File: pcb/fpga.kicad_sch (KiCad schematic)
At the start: 0 parts

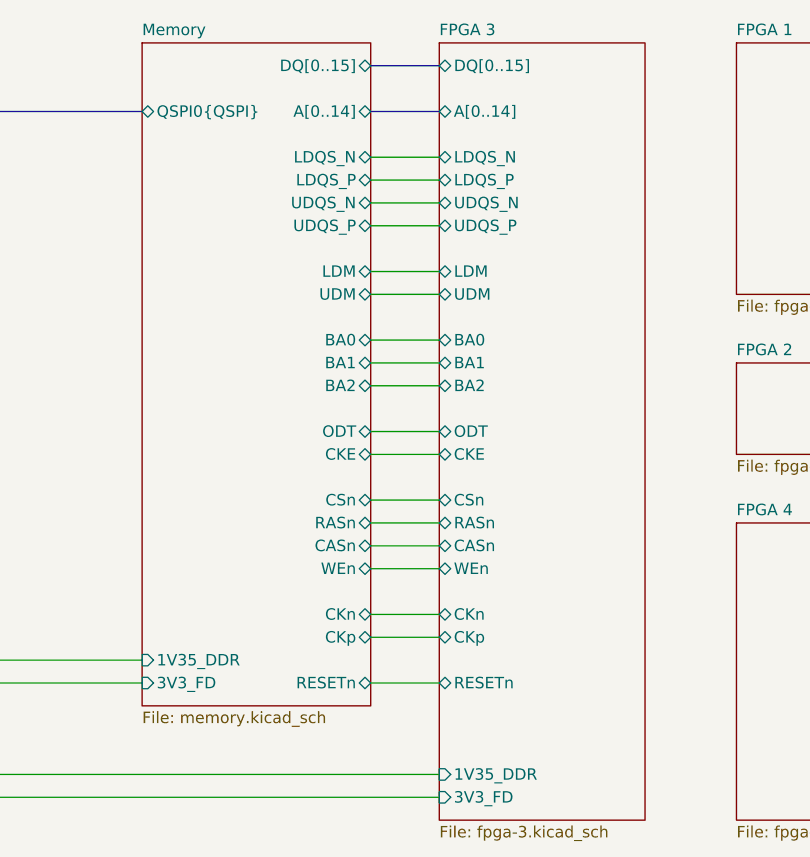
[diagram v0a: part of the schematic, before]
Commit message: added mig ddr pinout constraints
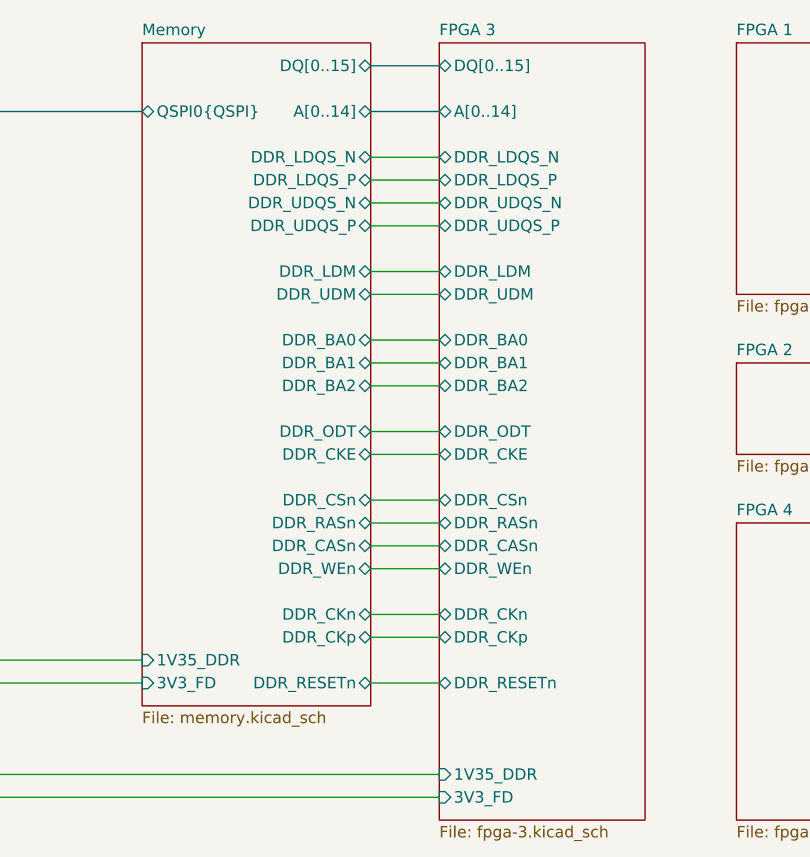
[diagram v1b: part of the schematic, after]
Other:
- sheet FPGA 3 ports: added DDR_BA0, DDR_BA1, DDR_BA2, DDR_CASn, DDR_CKE, DDR_CKn, DDR_CKp, DDR_CSn, DDR_LDM, DDR_LDQS_N, DDR_LDQS_P, DDR_ODT, DDR_RASn, DDR_RESETn, DDR_UDM, DDR_UDQS_N, DDR_UDQS_P, DDR_WEn; removed BA0, BA1, BA2, CASn, CKE, CKn, CKp, CSn, LDM, LDQS_N, LDQS_P, ODT, RASn, RESETn, UDM, UDQS_N, UDQS_P, WEn
- sheet Memory ports: added DDR_BA0, DDR_BA1, DDR_BA2, DDR_CASn, DDR_CKE, DDR_CKn, DDR_CKp, DDR_CSn, DDR_LDM, DDR_LDQS_N, DDR_LDQS_P, DDR_ODT, DDR_RASn, DDR_RESETn, DDR_UDM, DDR_UDQS_N, DDR_UDQS_P, DDR_WEn; removed BA0, BA1, BA2, CASn, CKE, CKn, CKp, CSn, LDM, LDQS_N, LDQS_P, ODT, RASn, RESETn, UDM, UDQS_N, UDQS_P, WEn
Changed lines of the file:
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@@
 			)
 		)
-		(pin "BA0" bidirectional
+		(pin "DDR_BA0" bidirectional
 			(at 132.08 86.36 180)
 			(effects
@@
 			)
 		)
-		(pin "BA1" bidirectional
+		(pin "DDR_BA1" bidirectional
 			(at 132.08 88.9 180)
 			(effects
@@
 			)
 		)
-		(pin "BA2" bidirectional
+		(pin "DDR_BA2" bidirectional
 			(at 132.08 91.44 180)
 			(effects
@@
 			)
 		)
-		(pin "CASn" bidirectional
+		(pin "DDR_CASn" bidirectional
 			(at 132.08 109.22 180)
 			(effects
@@
 			)
 		)
-		(pin "CKE" bidirectional
+		(pin "DDR_CKE" bidirectional
 			(at 132.08 99.06 180)
 			(effects
@@
 			)
 		)
-		(pin "CKn" bidirectional
+		(pin "DDR_CKn" bidirectional
 			(at 132.08 116.84 180)
 			(effects
@@
 			)
 		)
-		(pin "CKp" bidirectional
+		(pin "DDR_CKp" bidirectional
 			(at 132.08 119.38 180)
 			(effects
@@
 			)
 		)
-		(pin "CSn" bidirectional
+		(pin "DDR_CSn" bidirectional
 			(at 132.08 104.14 180)
 			(effects
@@
 			)
 		)
-		(pin "LDM" bidirectional
+		(pin "DDR_LDM" bidirectional
 			(at 132.08 78.74 180)
 			(effects
@@
 			)
 		)
-		(pin "LDQS_N" bidirectional
+		(pin "DDR_LDQS_N" bidirectional
 			(at 132.08 66.04 180)
 			(effects
@@
 			)
 		)
-		(pin "LDQS_P" bidirectional
+		(pin "DDR_LDQS_P" bidirectional
 			(at 132.08 68.58 180)
 			(effects
@@
 			)
 		)
-		(pin "ODT" bidirectional
+		(pin "DDR_ODT" bidirectional
 			(at 132.08 96.52 180)
 			(effects
@@
 			)
 		)
-		(pin "RASn" bidirectional
+		(pin "DDR_RASn" bidirectional
 			(at 132.08 106.68 180)
 			(effects
@@
 			)
 		)
-		(pin "RESETn" bidirectional
+		(pin "DDR_RESETn" bidirectional
 			(at 132.08 124.46 180)
 			(effects
@@
 			)
 		)
-		(pin "UDM" bidirectional
+		(pin "DDR_UDM" bidirectional
 			(at 132.08 81.28 180)
 			(effects
@@
 			)
 		)
-		(pin "UDQS_N" bidirectional
+		(pin "DDR_UDQS_N" bidirectional
 			(at 132.08 71.12 180)
 			(effects
@@
 			)
 		)
-		(pin "UDQS_P" bidirectional
+		(pin "DDR_UDQS_P" bidirectional
 			(at 132.08 73.66 180)
 			(effects
@@
 			)
 		)
-		(pin "WEn" bidirectional
+		(pin "DDR_WEn" bidirectional
 			(at 132.08 111.76 180)
 			(effects
@@
 			)
 		)
-		(pin "BA0" bidirectional
+		(pin "DDR_BA0" bidirectional
 			(at 124.46 86.36 0)
 			(effects
@@
 			)
 		)
-		(pin "BA1" bidirectional
+		(pin "DDR_BA1" bidirectional
 			(at 124.46 88.9 0)
 			(effects
@@
 			)
 		)
-		(pin "BA2" bidirectional
+		(pin "DDR_BA2" bidirectional
 			(at 124.46 91.44 0)
 			(effects
@@
 			)
 		)
-		(pin "CASn" bidirectional
+		(pin "DDR_CASn" bidirectional
 			(at 124.46 109.22 0)
 			(effects
@@
 			)
 		)
-		(pin "CKE" bidirectional
+		(pin "DDR_CKE" bidirectional
 			(at 124.46 99.06 0)
 			(effects
@@
 			)
 		)
-		(pin "CKn" bidirectional
+		(pin "DDR_CKn" bidirectional
 			(at 124.46 116.84 0)
 			(effects
@@
 			)
 		)
-		(pin "CKp" bidirectional
+		(pin "DDR_CKp" bidirectional
 			(at 124.46 119.38 0)
 			(effects
@@
 			)
 		)
-		(pin "CSn" bidirectional
+		(pin "DDR_CSn" bidirectional
 			(at 124.46 104.14 0)
 			(effects
@@
 			)
 		)
-		(pin "LDM" bidirectional
+		(pin "DDR_LDM" bidirectional
 			(at 124.46 78.74 0)
 			(effects
@@
 			)
 		)
-		(pin "LDQS_N" bidirectional
+		(pin "DDR_LDQS_N" bidirectional
 			(at 124.46 66.04 0)
 			(effects
@@
 			)
 		)
-		(pin "LDQS_P" bidirectional
+		(pin "DDR_LDQS_P" bidirectional
 			(at 124.46 68.58 0)
 			(effects
@@
 			)
 		)
-		(pin "ODT" bidirectional
+		(pin "DDR_ODT" bidirectional
 			(at 124.46 96.52 0)
 			(effects
@@
 			)
 		)
-		(pin "RASn" bidirectional
+		(pin "DDR_RASn" bidirectional
 			(at 124.46 106.68 0)
 			(effects
@@
 			)
 		)
-		(pin "RESETn" bidirectional
+		(pin "DDR_RESETn" bidirectional
 			(at 124.46 124.46 0)
 			(effects
@@
 			)
 		)
-		(pin "UDM" bidirectional
+		(pin "DDR_UDM" bidirectional
 			(at 124.46 81.28 0)
 			(effects
@@
 			)
 		)
-		(pin "UDQS_N" bidirectional
+		(pin "DDR_UDQS_N" bidirectional
 			(at 124.46 71.12 0)
 			(effects
@@
 			)
 		)
-		(pin "UDQS_P" bidirectional
+		(pin "DDR_UDQS_P" bidirectional
 			(at 124.46 73.66 0)
 			(effects
@@
 			)
 		)
-		(pin "WEn" bidirectional
+		(pin "DDR_WEn" bidirectional
 			(at 124.46 111.76 0)
 			(effects

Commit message: real ddr pinout done
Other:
- sheet FPGA 3 ports: added DDR_CK_N, DDR_CK_P; removed DDR_CKn, DDR_CKp
- sheet Memory ports: added DDR_CK_N, DDR_CK_P; removed DDR_CKn, DDR_CKp

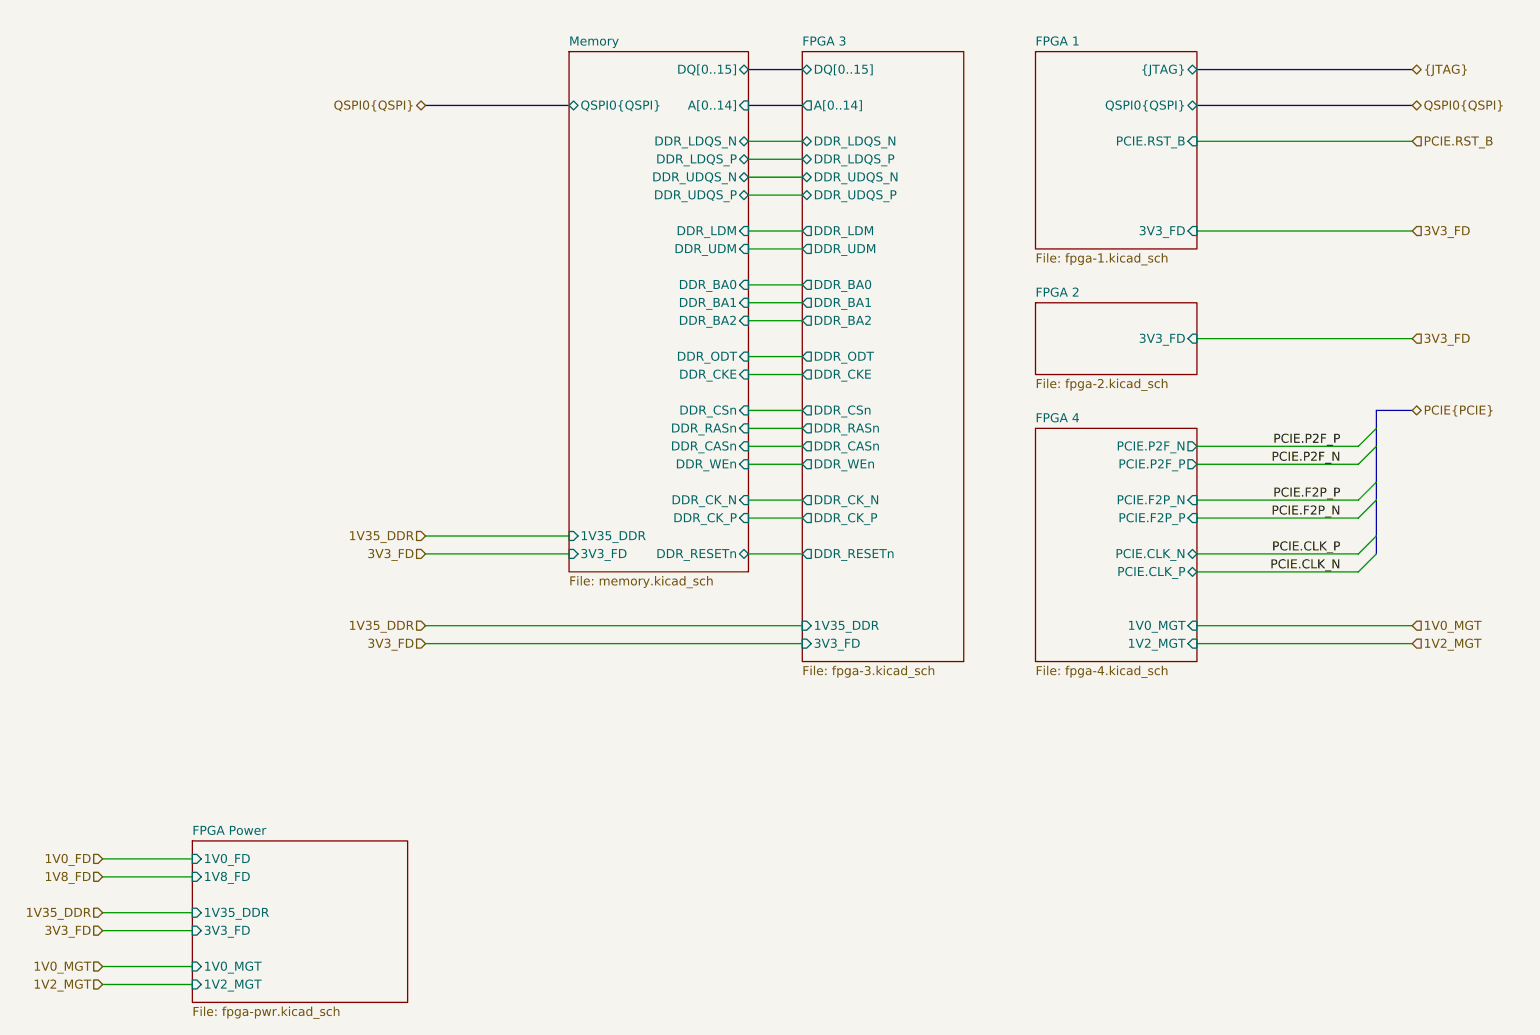
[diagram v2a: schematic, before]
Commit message: restructured power, power plane layout
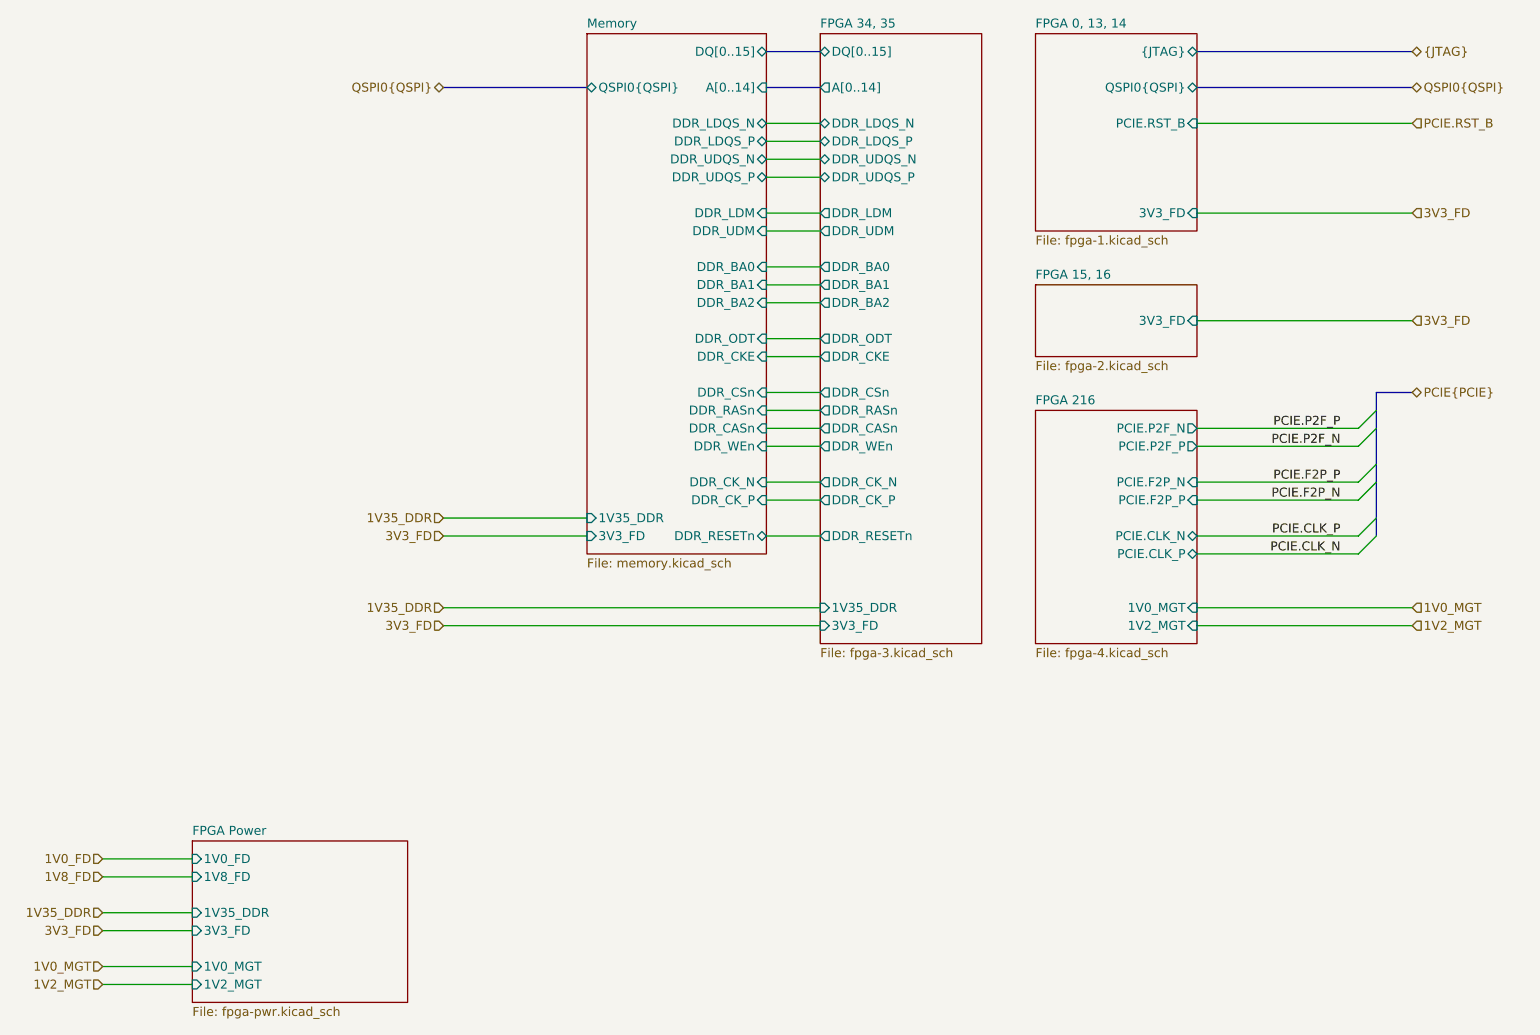
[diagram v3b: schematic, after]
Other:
- sheet FPGA 1 renamed FPGA 0, 13, 14
- sheet FPGA 2 renamed FPGA 15, 16
- sheet FPGA 3 renamed FPGA 34, 35
- sheet FPGA 4 renamed FPGA 216
